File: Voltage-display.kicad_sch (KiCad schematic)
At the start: 24 parts, among them J1 Conn_01x02, J2 Conn_01x02, Q1 DMP2035UQ-7, SW1 SW_SPST, U1 AMC1311BQDWVQ1, U2 R05CT05S-R

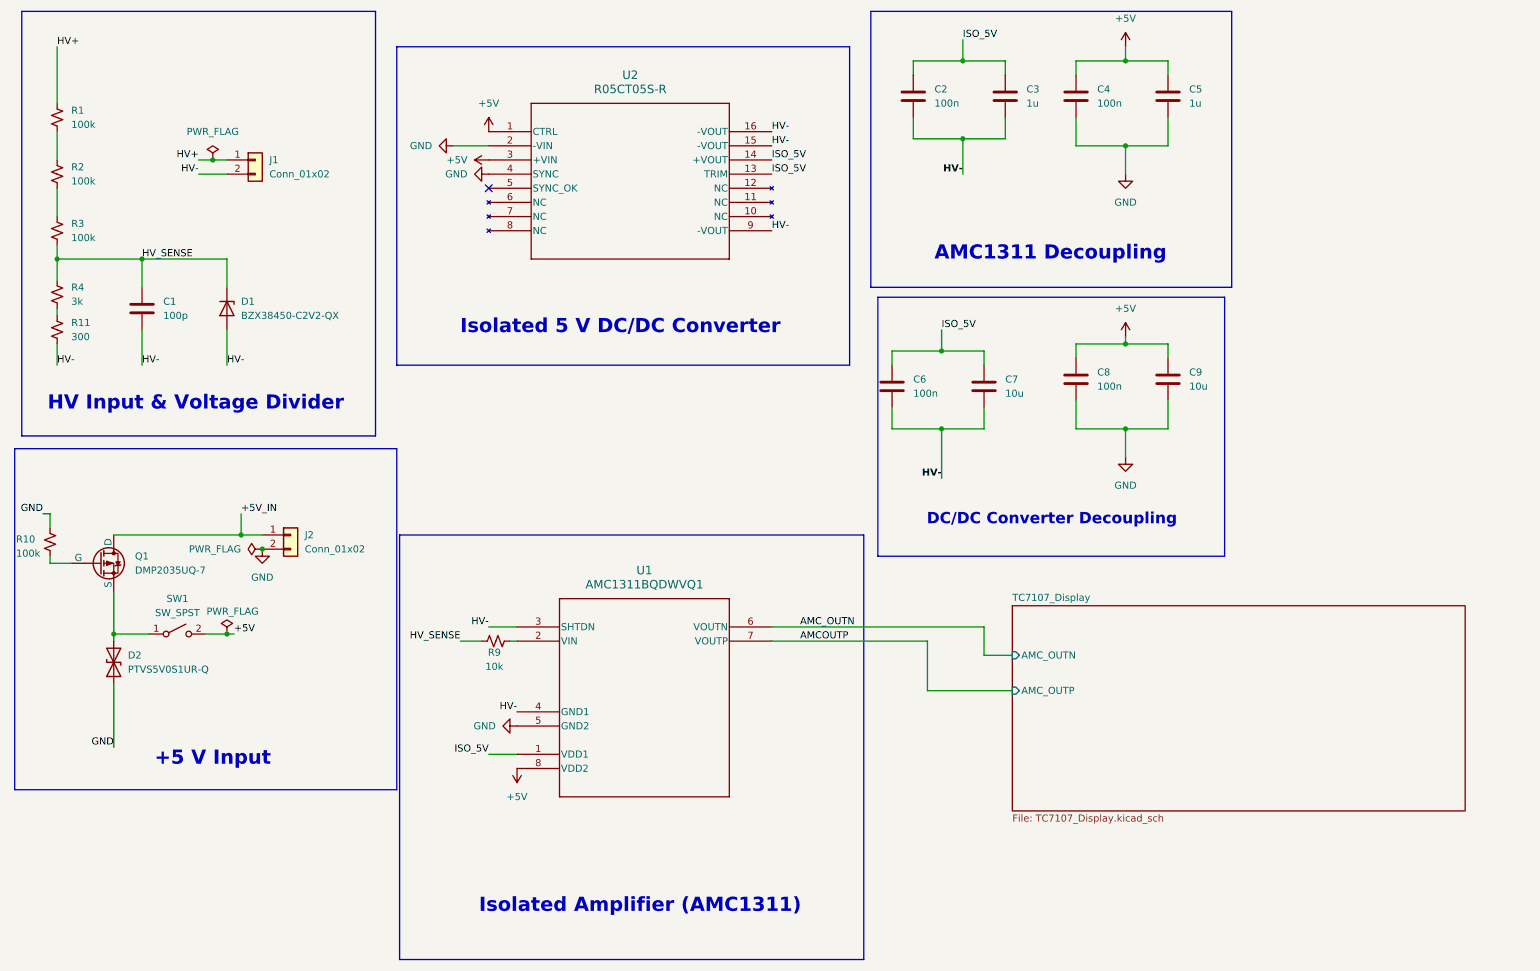
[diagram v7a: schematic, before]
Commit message: Replaced the AMC1311 and RECOME with AMC3311
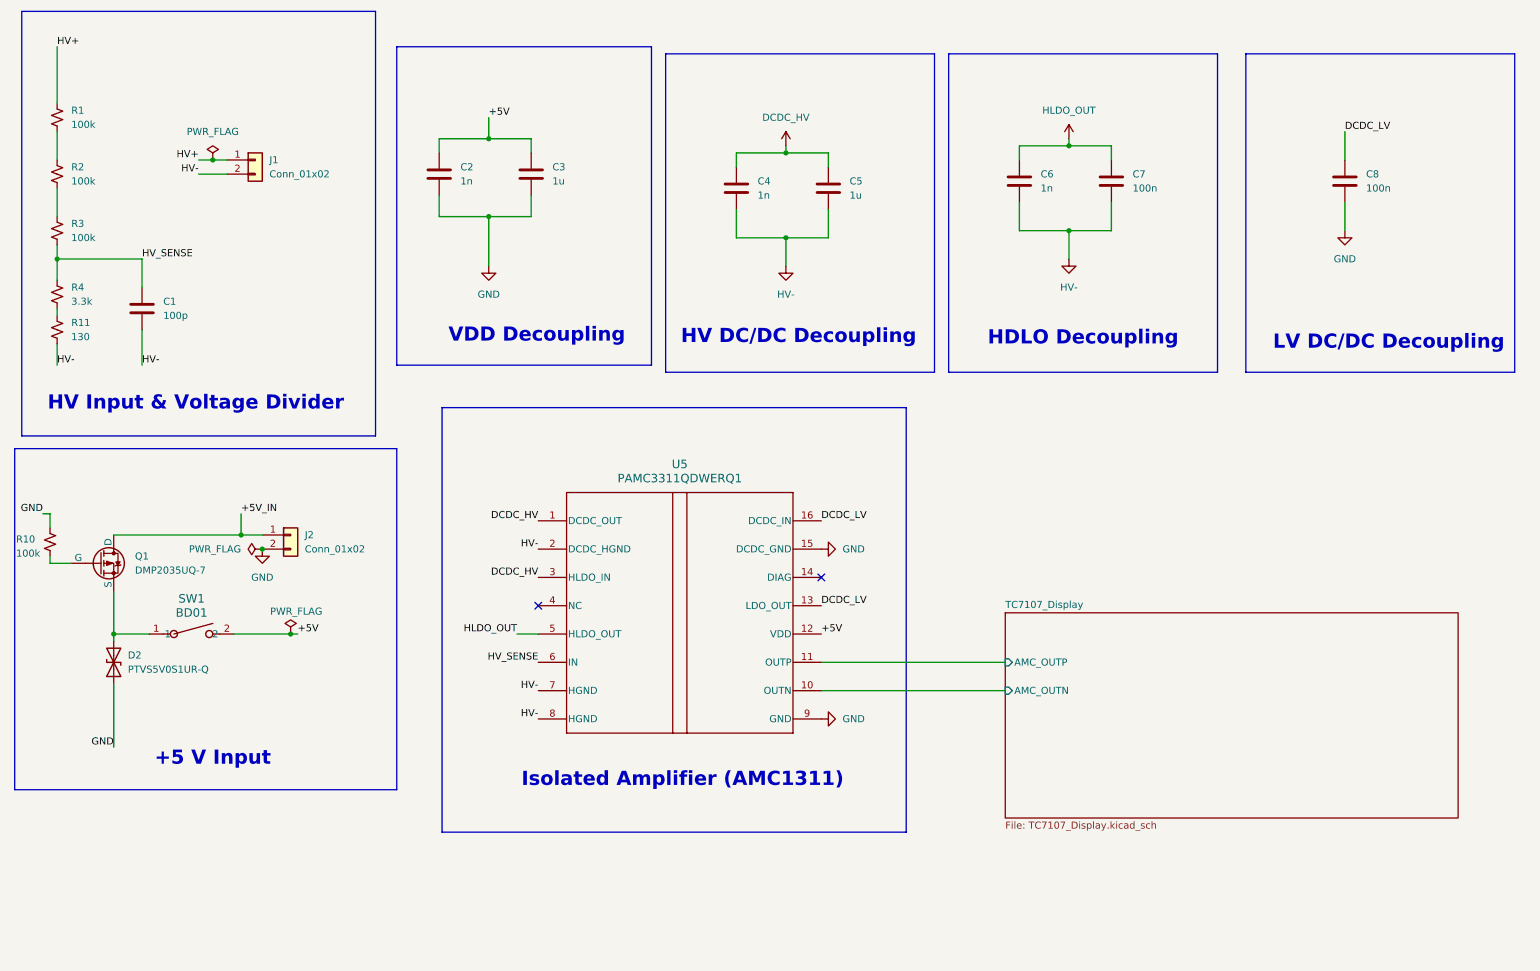
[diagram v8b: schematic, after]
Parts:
- removed C9: 10u, Capacitor_SMD:C_1206_3216Metric_Pad1.33x1.80mm_HandSolder, symbol Device:C
- removed D1: BZX38450-C2V2-QX, Diode_SMD:D_SOD-323_HandSoldering, symbol Device:D_Zener
- removed R9: 10k, Resistor_SMD:R_1206_3216Metric_Pad1.30x1.75mm_HandSolder, symbol Device:R_Small_US
- removed SW1: SW_SPST, symbol Switch:SW_SPST
- removed U1: AMC1311BQDWVQ1, ul_AMC1311BQDWVQ1_footprints:DWV8_TEX, symbol AMC1311:AMC1311BQDWVQ1
- removed U2: R05CT05S-R, R05CT055_R_footprints:SMD_16_10.3X7.5X2.6_RCP, symbol RECOM R05CT05S-R:R05CT05S-R
- added SW1: BD01, ul_BD01_footprints:SW_BD01_CNK, symbol ul_BD01:BD01
- added U5: PAMC3311QDWERQ1, ul_PAMC3311QDWERQ1_footprints:DWE0016A-IPC_A, symbol AMC3311-Q1:PAMC3311QDWERQ1
- C2, C4, C6: value 100n -> 1n
- C3, C5, C8: footprint Capacitor_SMD:C_0805_2012Metric_Pad1.18x1.45mm_HandSolder -> Capacitor_SMD:C_1206_3216Metric_Pad1.33x1.80mm_HandSolder
- C7: value 10u -> 100n
- R11: value 300 -> 130
- R4: value 3k -> 3.3k
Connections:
- net +5V: now also C2.1, C3.1, SW1.2, U5.12 (VDD); no longer C4.1, C5.1, C8.1
- net GND: now also C2.2, C3.2, U5.15 (DCDC_GND), U5.9 (GND); no longer C4.2, C5.2
- net HV-: now also C4.2, C5.2, U5.2 (DCDC_HGND), U5.7 (HGND), U5.8 (HGND); no longer C2.2, C3.2
- net HV_SENSE: now also U5.6 (IN)
- net at D2.2 (A2), Q1.3 (S): now also SW1.1
- net ISO_5V renamed HLDO_OUT
- net HLDO_OUT: now also U5.5 (HLDO_OUT); no longer C2.1, C3.1
- new net DCDC_HV: C4.1, C5.1, U5.1 (DCDC_OUT), U5.3 (HLDO_IN)
- new net DCDC_LV: C8.1, U5.13 (LDO_OUT), U5.16 (DCDC_IN)
- new net TC7107_Display/AMC_OUTN: U5.10 (OUTN)
- new net TC7107_Display/AMC_OUTP: U5.11 (OUTP)
- no-connect marks 1 -> 2
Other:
- note added: "HDLO Decoupling"
- note added: "HV DC/DC Decoupling"
- note added: "LV DC/DC Decoupling"
- note added: "VDD Decoupling"
- note removed: "AMC1311 Decoupling"
- note removed: "DC/DC Converter Decoupling"
- note removed: "Isolated 5 V DC/DC Converter"
